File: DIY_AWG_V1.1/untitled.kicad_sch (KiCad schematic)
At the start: 61 parts, among them U1 AMS1117-3.3, U2 ADP7118ARDZ-3.3-R7, U3 ADP7118ARDZ-3.3-R7, U4 TPS7A3301RGWR, U5 TPS7A4701RGWR, U6 TPS7A3301RGWR, U7 TPS7A4701RGWR

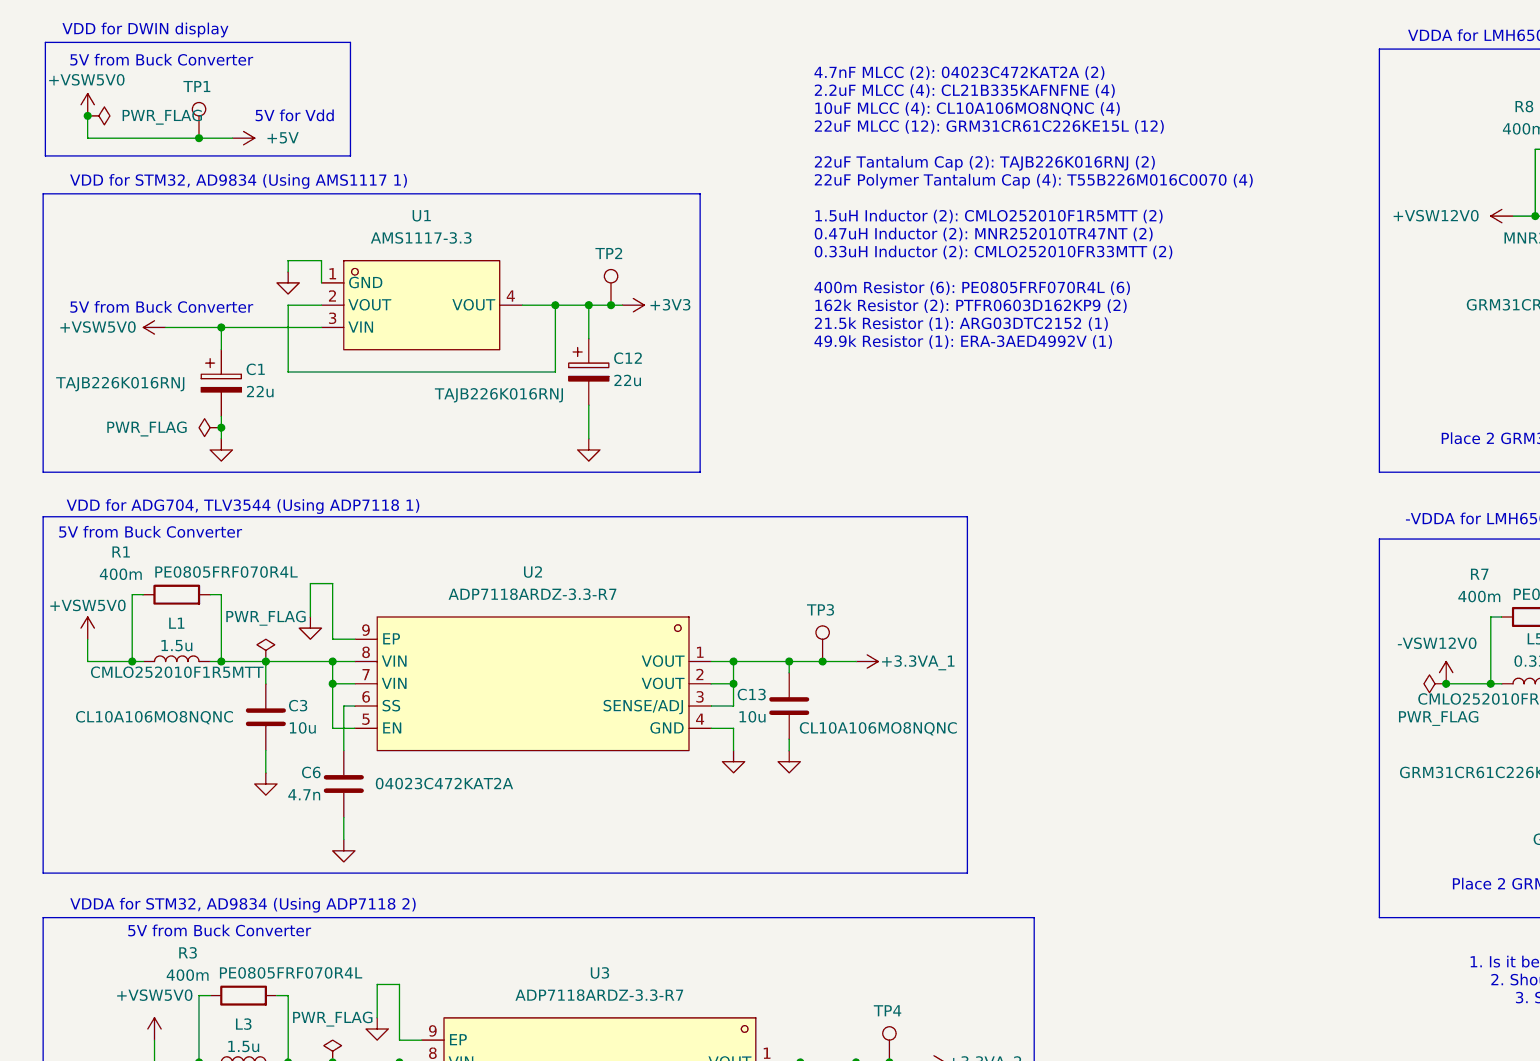
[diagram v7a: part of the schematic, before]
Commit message: Updated schematic footprints
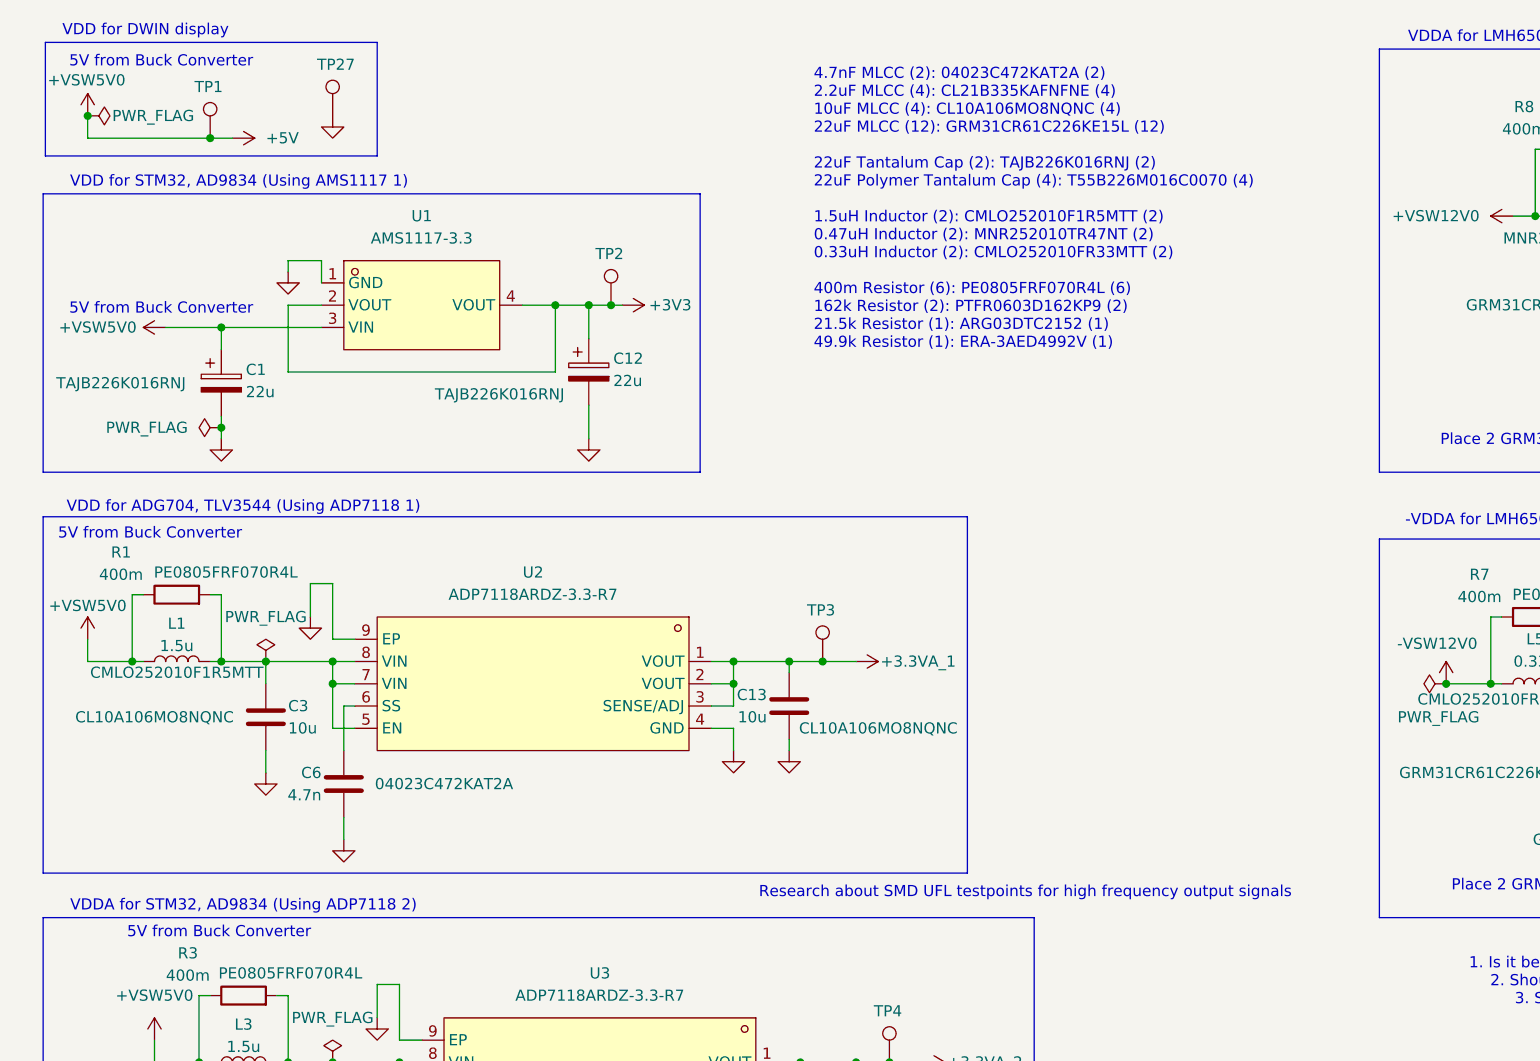
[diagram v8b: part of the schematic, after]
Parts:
- added TP27: TestPoint, TestPoint:TestPoint_Pad_D2.0mm, symbol Connector:TestPoint
- TP1, TP2, TP3: footprint (none) -> TestPoint:TestPoint_Pad_D2.0mm
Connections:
- net GND: now also TP27.1
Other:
- note added: "Research about SMD UFL testpoints for high frequency output signals"
- note removed: "5V for Vdd"
- moved on the sheet: TP1
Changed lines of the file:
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@@
 	(rectangle
 		(start 15.494 18.288)
-		(end 50.292 31.242)
+		(end 53.34 31.242)
 		(stroke
 			(width 0)
@@
 		)
 	)
-	(text "4.7nF MLCC (2): 04023C472KAT2A (2)\n2.2uF MLCC (4): CL21B335KAFNFNE (4)\n10uF MLCC (4): CL10A106MO8NQNC (4)\n22uF MLCC (12): GRM31CR61C226KE15L (12)\n\n22uF Tantalum Cap (2): TAJB226K016RNJ (2)\n22uF Polymer Tantalum Cap (4): T55B226M016C0070 (4)\n\n1.5uH Inductor (2): CMLO252010F1R5MTT (2)\n0.47uH Inductor (2): MNR252010TR47NT (2)\n0.33uH Inductor (2): CMLO252010FR33MTT (2)\n\n400m Resistor (6): PE0805FRF070R4L (6)\n162k Resistor (2): PTFR0603D162KP9 (2)\n21.5k Resistor (1): ARG03DTC2152 (1)\n49.9k Resistor (1): ERA-3AED4992V (1)"
+	(text "Research about SMD UFL testpoints for high frequency output signals\n"
 		(exclude_from_sim no)
-		(at 103.124 37.338 0)
+		(at 127.254 115.316 0)
 		(effects
 			(font
 				(size 1.27 1.27)
 			)
-			(justify left)
 		)
 	)
-	(text "Place 2 GRM31CR61C226KE15L in parallel\n(eff. cap - 10uF)"
+	(text "4.7nF MLCC (2): 04023C472KAT2A (2)\n2.2uF MLCC (4): CL21B335KAFNFNE (4)\n10uF MLCC (4): CL10A106MO8NQNC (4)\n22uF MLCC (12): GRM31CR61C226KE15L (12)\n\n22uF Tantalum Cap (2): TAJB226K016RNJ (2)\n22uF Polymer Tantalum Cap (4): T55B226M016C0070 (4)\n\n1.5uH Inductor (2): CMLO252010F1R5MTT (2)\n0.47uH Inductor (2): MNR252010TR47NT (2)\n0.33uH Inductor (2): CMLO252010FR33MTT (2)\n\n400m Resistor (6): PE0805FRF070R4L (6)\n162k Resistor (2): PTFR0603D162KP9 (2)\n21.5k Resistor (1): ARG03DTC2152 (1)\n49.9k Resistor (1): ERA-3AED4992V (1)"
 		(exclude_from_sim no)
-		(at 194.31 115.57 0)
+		(at 103.124 37.338 0)
 		(effects
 			(font
 				(size 1.27 1.27)
 			)
+			(justify left)
 		)
 	)
-	(text "5V for Vdd\n"
+	(text "Place 2 GRM31CR61C226KE15L in parallel\n(eff. cap - 10uF)"
 		(exclude_from_sim no)
-		(at 43.942 26.924 0)
+		(at 194.31 115.57 0)
 		(effects
 			(font
@@
 	)
 	(junction
-		(at 33.02 29.21)
-		(diameter 0)
-		(color 0 0 0 0)
-	)
-	(junction
 		(at 313.69 90.17)
 		(diameter 0)
@@
 	)
 	(junction
+		(at 34.29 29.21)
+		(diameter 0)
+		(color 0 0 0 0)
+	)
+	(junction
 		(at 143.51 231.14)
 		(diameter 0)
@@
 	(wire
 		(pts
-			(xy 33.02 29.21) (xy 36.83 29.21)
-		)
-		(stroke
-			(width 0)
-			(type default)
-		)
-	)
-	(wire
-		(pts
 			(xy 99.06 139.7) (xy 101.6 139.7)
 		)
@@
 	(wire
 		(pts
+			(xy 34.29 29.21) (xy 36.83 29.21)
+		)
+		(stroke
+			(width 0)
+			(type default)
+		)
+	)
+	(wire
+		(pts
 			(xy 20.32 86.36) (xy 20.32 88.9)
 		)
@@
 	(wire
 		(pts
-			(xy 20.32 29.21) (xy 33.02 29.21)
+			(xy 20.32 29.21) (xy 34.29 29.21)
 		)
 		(stroke
@@
 		(in_pos_files yes)
 		(dnp no)
-		(fields_autoplaced yes)
 		(property "Reference" "#FLG01"
 			(at 22.225 26.67 0)
@@
 		)
 		(property "Value" "PWR_FLAG"
-			(at 24.13 26.6699 90)
+			(at 23.114 26.67 90)
 			(show_name no)
 			(do_not_autoplace no)
@@
 	)
 	(symbol
+		(lib_id "Connector:TestPoint")
+		(at 48.26 26.67 0)
+		(unit 1)
+		(body_style 1)
+		(exclude_from_sim no)
+		(in_bom yes)
+		(on_board yes)
+		(in_pos_files yes)
+		(dnp no)
+		(property "Reference" "TP27"
+			(at 46.482 20.828 0)
+			(show_name no)
+			(do_not_autoplace no)
+			(effects
+				(font
+					(size 1.27 1.27)
+				)
+				(justify left)
+			)
+		)
+		(property "Value" "TestPoint"
+			(at 44.196 21.082 0)
+			(hide yes)
+			(show_name no)
+			(do_not_autoplace no)
+			(effects
+				(font
+					(size 1.27 1.27)
+				)
+				(justify left)
+			)
+		)
+		(property "Footprint" "TestPoint:TestPoint_Pad_D2.0mm"
+			(at 53.34 26.67 0)
+			(hide yes)
+			(show_name no)
+			(do_not_autoplace no)
+			(effects
+				(font
+					(size 1.27 1.27)
+				)
+			)
+		)
+		(property "Datasheet" ""
+			(at 53.34 26.67 0)
+			(hide yes)
+			(show_name no)
+			(do_not_autoplace no)
+			(effects
+				(font
+					(size 1.27 1.27)
+				)
+			)
+		)
+		(property "Description" "test point"
+			(at 48.26 26.67 0)
+			(hide yes)
+			(show_name no)
+			(do_not_autoplace no)
+			(effects
+				(font
+					(size 1.27 1.27)
+				)
+			)
+		)
+		(pin "1"
+		)
+		(instances
+			(project "DIY_AWG_V1.1"
+				(path "/508078af-d961-4af3-840e-a064a9f8d5bc/8acbd35e-0359-4140-a5a5-b9cabf9b139d"
+					(reference "TP27")
+					(unit 1)
+				)
+			)
+		)
+	)
+	(symbol
 		(lib_id "power:PWR_FLAG")
 		(at 200.66 38.1 0)
@@
 			)
 		)
-		(property "Footprint" ""
+		(property "Footprint" "TestPoint:TestPoint_Pad_D2.0mm"
 			(at 109.22 88.9 0)
 			(hide yes)
@@
 	)
 	(symbol
+		(lib_id "power:GND")
+		(at 48.26 26.67 0)
+		(unit 1)
+		(body_style 1)
+		(exclude_from_sim no)
+		(in_bom yes)
+		(on_board yes)
+		(in_pos_files yes)
+		(dnp no)
+		(fields_autoplaced yes)
+		(property "Reference" "#PWR0181"
+			(at 48.26 33.02 0)
+			(hide yes)
+			(show_name no)
+			(do_not_autoplace no)
+			(effects
+				(font
+					(size 1.27 1.27)
+				)
+			)
+		)
+		(property "Value" "GND"
+			(at 48.26 31.75 0)
+			(hide yes)
+			(show_name no)
+			(do_not_autoplace no)
+			(effects
+				(font
+					(size 1.27 1.27)
+				)
+			)
+		)
+		(property "Footprint" ""
+			(at 48.26 26.67 0)
+			(hide yes)
+			(show_name no)
+			(do_not_autoplace no)
+			(effects
+				(font
+					(size 1.27 1.27)
+				)
+			)
+		)
+		(property "Datasheet" ""
+			(at 48.26 26.67 0)
+			(hide yes)
+			(show_name no)
+			(do_not_autoplace no)
+			(effects
+				(font
+					(size 1.27 1.27)
+				)
+			)
+		)
+		(property "Description" "Power symbol creates a global label with name \"GND\" , ground"
+			(at 48.26 26.67 0)
+			(hide yes)
+			(show_name no)
+			(do_not_autoplace no)
+			(effects
+				(font
+					(size 1.27 1.27)
+				)
+			)
+		)
+		(pin "1"
+		)
+		(instances
+			(project "DIY_AWG_V1.1"
+				(path "/508078af-d961-4af3-840e-a064a9f8d5bc/8acbd35e-0359-4140-a5a5-b9cabf9b139d"
+					(reference "#PWR0181")
+					(unit 1)
+				)
+			)
+		)
+	)
+	(symbol
 		(lib_id "Device:R")
 		(at 132.08 234.95 0)
@@
 			)
 		)
-		(property "Footprint" ""
+		(property "Footprint" "TestPoint:TestPoint_Pad_D2.0mm"
 			(at 85.09 48.26 0)
 			(hide yes)
@@
 	(symbol
 		(lib_id "Connector:TestPoint")
-		(at 33.02 29.21 0)
+		(at 34.29 29.21 0)
 		(unit 1)
 		(body_style 1)
@@
 		(dnp no)
 		(property "Reference" "TP1"
-			(at 31.242 23.368 0)
+			(at 32.512 23.368 0)
 			(show_name no)
 			(do_not_autoplace no)
@@
 		)
 		(property "Value" "TestPoint"
-			(at 28.956 23.622 0)
+			(at 30.226 23.622 0)
 			(hide yes)
 			(show_name no)
@@
 			)
 		)
-		(property "Footprint" ""
-			(at 38.1 29.21 0)
+		(property "Footprint" "TestPoint:TestPoint_Pad_D2.0mm"
+			(at 39.37 29.21 0)
 			(hide yes)
 			(show_name no)
@@
 		)
 		(property "Datasheet" ""
-			(at 38.1 29.21 0)
+			(at 39.37 29.21 0)
 			(hide yes)
 			(show_name no)
@@
 		)
 		(property "Description" "test point"
-			(at 33.02 29.21 0)
+			(at 34.29 29.21 0)
 			(hide yes)
 			(show_name no)
